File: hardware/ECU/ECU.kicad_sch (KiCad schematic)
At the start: 112 parts, among them IC1 IR4427SPBF, IC2 EL357NB_TA_-G, IC3 EL357NB_TA_-G, IC4 ESP32-S3-WROOM-1U-N8R8, IC5 EL357NB_TA_-G, J1 AQS, J2 TFP09-2-12B, J3 CAM_SENSOR, J4 USB_B, J5 BATTERY, J6 GATEs, J7 ISC Control, J8 CAPTURE_TRG, Q1 RJP63K2, Q3 RJP63K2, Q4 RJP63K2, SW1 RESET BTN, SW2 ZERO BTN, U1 LM2576S-5, U2 AMS1117-3.3, U3 L293D, U4 ADS1115IDGS, U5 ADS1115IDGS, U6 INA180A3, U7 SRV05-4

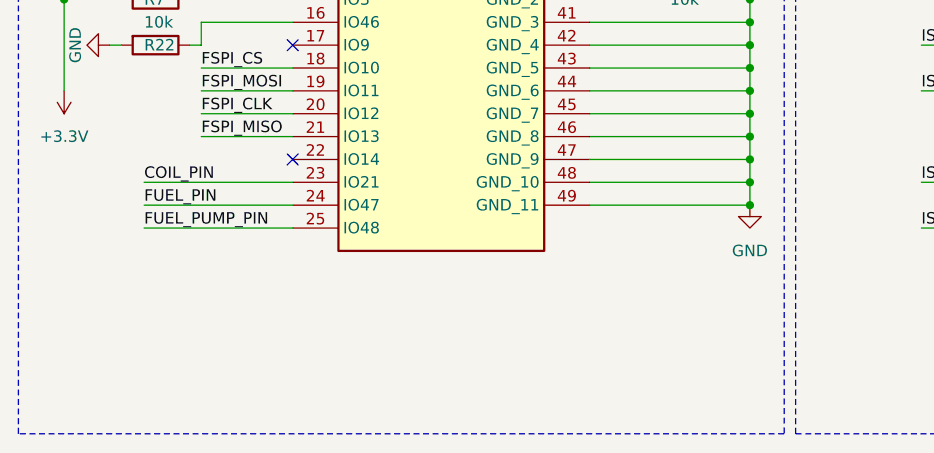
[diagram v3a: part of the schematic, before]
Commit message: fix gerber file containing deleted layers
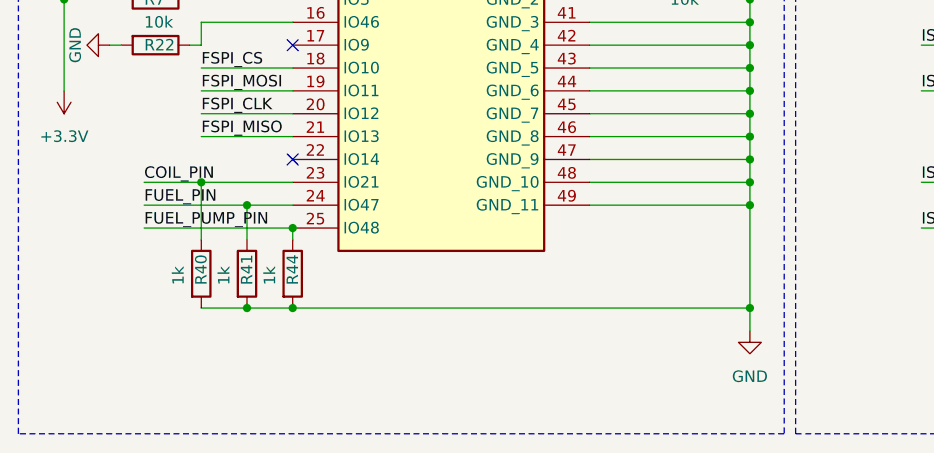
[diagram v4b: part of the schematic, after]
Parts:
- added R40, R41, R44: 1k, Resistor_SMD:R_0603_1608Metric_Pad0.98x0.95mm_HandSolder, symbol Device:R
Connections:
- net COIL_PIN: now also R40.1
- net FUEL_PIN: now also R41.1
- net FUEL_PUMP_PIN: now also R44.1
- net GND: now also R40.2, R41.2, R44.2
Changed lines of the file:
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@@
   (junction (at 261.62 132.08) (diameter 0) (color 0 0 0 0)
   )
+  (junction (at 38.1 171.45) (diameter 0) (color 0 0 0 0)
+  )
+  (junction (at 33.02 168.91) (diameter 0) (color 0 0 0 0)
+  )
   (junction (at 255.27 95.25) (diameter 0) (color 0 0 0 0)
   )
@@
   (junction (at 135.89 132.08) (diameter 0) (color 0 0 0 0)
   )
+  (junction (at 38.1 182.88) (diameter 0) (color 0 0 0 0)
+  )
   (junction (at 161.29 95.25) (diameter 0) (color 0 0 0 0)
   )
@@
   (junction (at 22.86 40.64) (diameter 0) (color 0 0 0 0)
   )
+  (junction (at 43.18 182.88) (diameter 0) (color 0 0 0 0)
+  )
   (junction (at 106.68 22.86) (diameter 0) (color 0 0 0 0)
   )
@@
   (junction (at 231.14 132.08) (diameter 0) (color 0 0 0 0)
   )
+  (junction (at 43.18 173.99) (diameter 0) (color 0 0 0 0)
+  )
   (junction (at 250.19 119.38) (diameter 0) (color 0 0 0 0)
   )
@@
   (junction (at 207.01 119.38) (diameter 0) (color 0 0 0 0)
   )
+  (junction (at 93.98 182.88) (diameter 0) (color 0 0 0 0)
+  )
   (junction (at 86.36 40.64) (diameter 0) (color 0 0 0 0)
   )
@@
     (stroke (width 0) (type default))
   )
+  (wire (pts (xy 38.1 171.45) (xy 38.1 175.26))
+    (stroke (width 0) (type default))
+  )
   (wire (pts (xy 30.48 118.11) (xy 43.18 118.11))
     (stroke (width 0) (type default))
@@
     (stroke (width 0) (type default))
   )
+  (wire (pts (xy 93.98 171.45) (xy 93.98 182.88))
+    (stroke (width 0) (type default))
+  )
   (wire (pts (xy 231.14 121.92) (xy 237.49 121.92))
     (stroke (width 0) (type default))
@@
     (stroke (width 0) (type default))
   )
+  (wire (pts (xy 38.1 171.45) (xy 43.18 171.45))
+    (stroke (width 0) (type default))
+  )
   (wire (pts (xy 156.21 93.98) (xy 156.21 95.25))
     (stroke (width 0) (type default))
@@
     (stroke (width 0) (type default))
   )
+  (wire (pts (xy 33.02 168.91) (xy 43.18 168.91))
+    (stroke (width 0) (type default))
+  )
   (wire (pts (xy 182.88 119.38) (xy 191.77 119.38))
     (stroke (width 0) (type default))
@@
     (stroke (width 0) (type default))
   )
+  (wire (pts (xy 38.1 182.88) (xy 43.18 182.88))
+    (stroke (width 0) (type default))
+  )
   (wire (pts (xy 116.84 66.04) (xy 116.84 81.28))
     (stroke (width 0) (type default))
@@
     (stroke (width 0) (type default))
   )
+  (wire (pts (xy 93.98 182.88) (xy 93.98 185.42))
+    (stroke (width 0) (type default))
+  )
   (wire (pts (xy 234.95 59.69) (xy 238.76 59.69))
     (stroke (width 0) (type default))
@@
     (stroke (width 0) (type default))
   )
+  (wire (pts (xy 43.18 182.88) (xy 93.98 182.88))
+    (stroke (width 0) (type default))
+  )
   (wire (pts (xy 231.14 132.08) (xy 243.84 132.08))
     (stroke (width 0) (type default))
@@
     (stroke (width 0) (type default))
   )
+  (wire (pts (xy 43.18 173.99) (xy 43.18 175.26))
+    (stroke (width 0) (type default))
+  )
   (wire (pts (xy 78.74 21.59) (xy 78.74 22.86))
     (stroke (width 0) (type default))
@@
     (stroke (width 0) (type default))
   )
-  (wire (pts (xy 26.67 168.91) (xy 43.18 168.91))
+  (wire (pts (xy 26.67 168.91) (xy 33.02 168.91))
     (stroke (width 0) (type default))
   )
@@
     (stroke (width 0) (type default))
   )
-  (wire (pts (xy 26.67 171.45) (xy 43.18 171.45))
+  (wire (pts (xy 26.67 171.45) (xy 38.1 171.45))
     (stroke (width 0) (type default))
   )
@@
     (stroke (width 0) (type default))
   )
+  (wire (pts (xy 33.02 182.88) (xy 38.1 182.88))
+    (stroke (width 0) (type default))
+  )
   (wire (pts (xy 74.93 34.29) (xy 74.93 40.64))
     (stroke (width 0) (type default))
@@
     (stroke (width 0) (type default))
   )
+  (wire (pts (xy 33.02 168.91) (xy 33.02 175.26))
+    (stroke (width 0) (type default))
+  )
   (wire (pts (xy 181.61 127) (xy 181.61 132.08))
     (stroke (width 0) (type default))
@@
     )
   )
-  (symbol (lib_id "power:GND") (at 93.98 171.45 0) (unit 1)
+  (symbol (lib_id "power:GND") (at 93.98 185.42 0) (unit 1)
     (in_bom yes) (on_board yes) (dnp no) (fields_autoplaced)
-    (property "Reference" "#PWR08" (at 93.98 177.8 0)
+    (property "Reference" "#PWR08" (at 93.98 191.77 0)
       (effects (font (size 1.27 1.27)) hide)
     )
-    (property "Value" "GND" (at 93.98 176.53 0)
+    (property "Value" "GND" (at 93.98 190.5 0)
       (effects (font (size 1.27 1.27)))
     )
-    (property "Footprint" "" (at 93.98 171.45 0)
+    (property "Footprint" "" (at 93.98 185.42 0)
       (effects (font (size 1.27 1.27)) hide)
     )
-    (property "Datasheet" "" (at 93.98 171.45 0)
+    (property "Datasheet" "" (at 93.98 185.42 0)
       (effects (font (size 1.27 1.27)) hide)
     )
@@
     )
   )
+  (symbol (lib_id "Device:R") (at 43.18 179.07 0) (unit 1)
+    (in_bom yes) (on_board yes) (dnp no)
+    (property "Reference" "R44" (at 43.18 180.34 90)
+      (effects (font (size 1.27 1.27)) (justify left))
+    )
+    (property "Value" "1k" (at 40.64 180.34 90)
+      (effects (font (size 1.27 1.27)) (justify left))
+    )
+    (property "Footprint" "Resistor_SMD:R_0603_1608Metric_Pad0.98x0.95mm_HandSolder" (at 41.402 179.07 90)
+      (effects (font (size 1.27 1.27)) hide)
+    )
+    (property "Datasheet" "~" (at 43.18 179.07 0)
+      (effects (font (size 1.27 1.27)) hide)
+    )
+    (pin "1")
+    (pin "2")
+    (instances
+      (project "ECU"
+        (path "/67ab37fa-126a-4ea1-a2e7-116539662db8"
+          (reference "R44") (unit 1)
+        )
+      )
+    )
+  )
   (symbol (lib_id "power:+5V") (at 118.11 143.51 90) (unit 1)
     (in_bom yes) (on_board yes) (dnp no) (fields_autoplaced)
@@
     )
   )
+  (symbol (lib_id "Device:R") (at 38.1 179.07 0) (unit 1)
+    (in_bom yes) (on_board yes) (dnp no)
+    (property "Reference" "R41" (at 38.1 180.34 90)
+      (effects (font (size 1.27 1.27)) (justify left))
+    )
+    (property "Value" "1k" (at 35.56 180.34 90)
+      (effects (font (size 1.27 1.27)) (justify left))
+    )
+    (property "Footprint" "Resistor_SMD:R_0603_1608Metric_Pad0.98x0.95mm_HandSolder" (at 36.322 179.07 90)
+      (effects (font (size 1.27 1.27)) hide)
+    )
+    (property "Datasheet" "~" (at 38.1 179.07 0)
+      (effects (font (size 1.27 1.27)) hide)
+    )
+    (pin "1")
+    (pin "2")
+    (instances
+      (project "ECU"
+        (path "/67ab37fa-126a-4ea1-a2e7-116539662db8"
+          (reference "R41") (unit 1)
+        )
+      )
+    )
+  )
   (symbol (lib_id "Device:R") (at 231.14 83.82 270) (unit 1)
     (in_bom yes) (on_board yes) (dnp no)
@@
         )
       )
+    )
+  )
+  (symbol (lib_id "Device:R") (at 33.02 179.07 0) (unit 1)
+    (in_bom yes) (on_board yes) (dnp no)
+    (property "Reference" "R40" (at 33.02 180.34 90)
+      (effects (font (size 1.27 1.27)) (justify left))
+    )
+    (property "Value" "1k" (at 30.48 180.34 90)
+      (effects (font (size 1.27 1.27)) (justify left))
+    )
+    (property "Footprint" "Resistor_SMD:R_0603_1608Metric_Pad0.98x0.95mm_HandSolder" (at 31.242 179.07 90)
+      (effects (font (size 1.27 1.27)) hide)
+    )
+    (property "Datasheet" "~" (at 33.02 179.07 0)
+      (effects (font (size 1.27 1.27)) hide)
+    )
+    (pin "1")
+    (pin "2")
+    (instances
+      (project "ECU"
+        (path "/67ab37fa-126a-4ea1-a2e7-116539662db8"
+          (reference "R40") (unit 1)
+        )
+      )
